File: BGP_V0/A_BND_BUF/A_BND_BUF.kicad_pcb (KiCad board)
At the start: 2 copper layers, 30 x 30 mm, 27 parts, among them J1 Conn_01x05, P1 CONN_01X02, P2 CONN_01X02, Q1 2SK208, Q2 2SK208, U1 OPA180

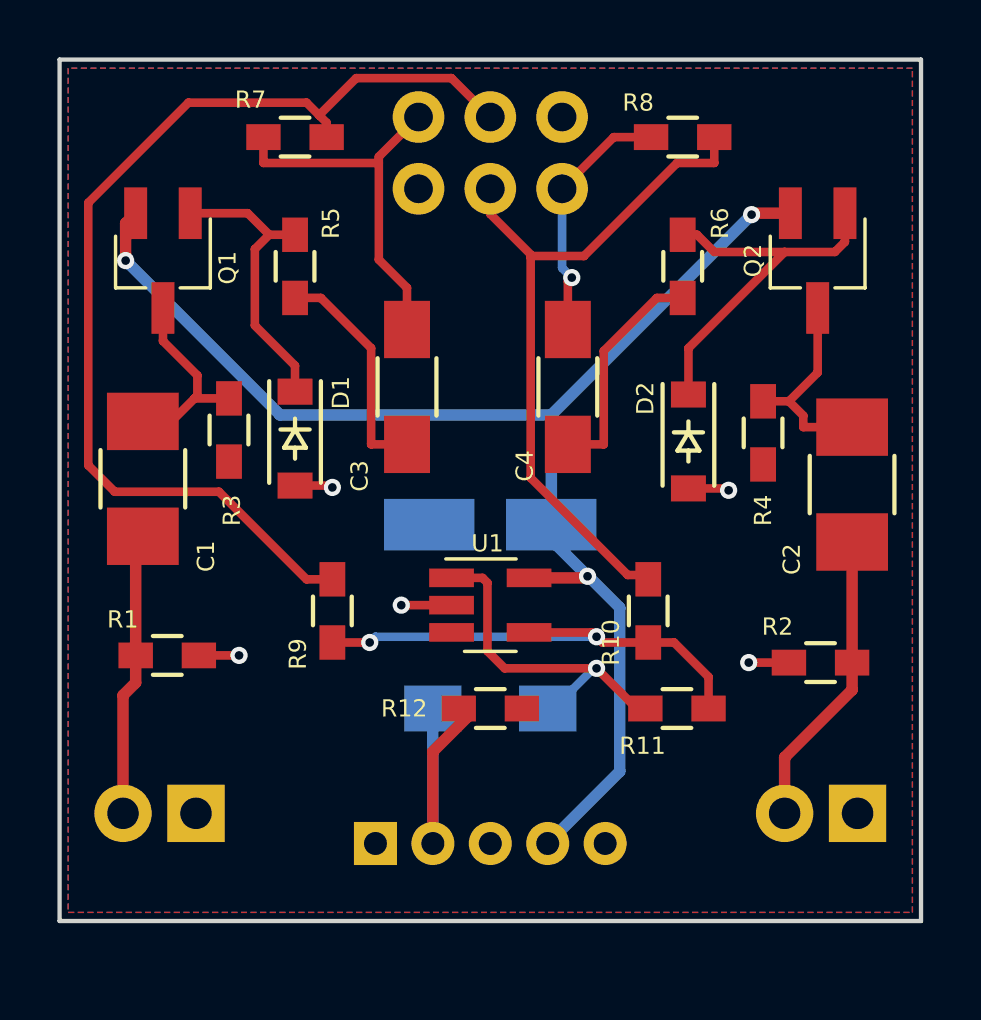
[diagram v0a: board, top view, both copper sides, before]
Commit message: Gerbers
Mainly getting gerbers ready.  Issue with pots overlapping other boards in silk screens - top and bottom.
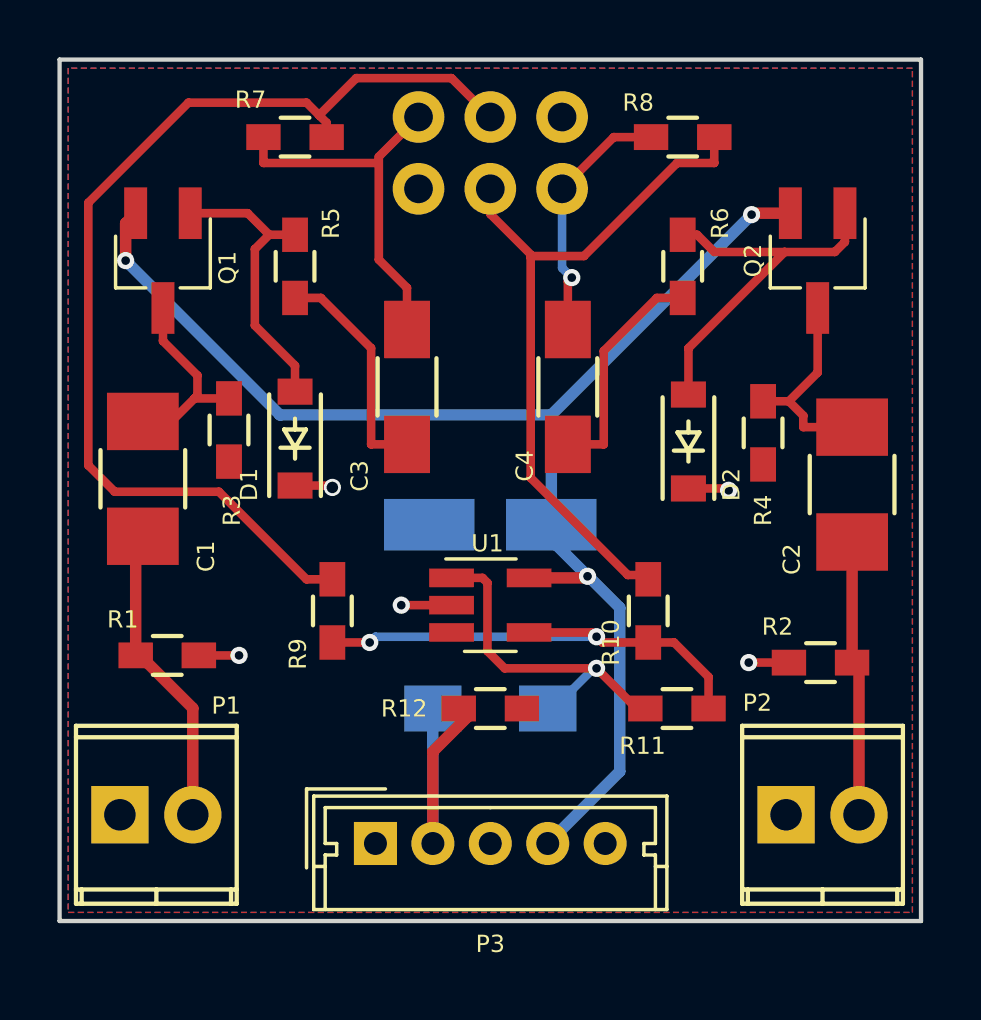
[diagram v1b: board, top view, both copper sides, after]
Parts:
- removed J1: Conn_01x05, Connectors_Molex:Molex_MicroLatch-53253-0570_05x2.00mm_Straight
- added P3: Conn_01x05, Connectors_Molex:Molex_MicroLatch-53253-0570_05x2.00mm_Straight, F.Cu at (147.0, 95.3)
- P1, P2: moved to F.Cu
- moved P1 2.65 mm to (138.1, 94.3), turned to 0 degrees
- moved P2 2.49 mm to (161.3, 94.3), turned to 0 degrees
- turned D1 to 90 degrees
- turned D2 to 90 degrees
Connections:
- D1 pad 1: Net-(D1-Pad1) -> Earth
- D1 pad 2: Earth -> Net-(D1-Pad2)
- D2 pad 1: Net-(D2-Pad1) -> Earth
- D2 pad 2: Earth -> Net-(D2-Pad2)
- Q1 pad 1: Net-(D1-Pad1) -> Net-(D1-Pad2)
- Q2 pad 1: Net-(D2-Pad1) -> Net-(D2-Pad2)
- R5 pad 2: Net-(D1-Pad1) -> Net-(D1-Pad2)
- R6 pad 2: Net-(D2-Pad1) -> Net-(D2-Pad2)
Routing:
- net Net-(D2-Pad2): track 0.00 -> 13.4 mm
- net Net-(D2-Pad1): track 13.4 -> 0.00 mm
- net Net-(D1-Pad2): track 0.00 -> 10.2 mm
- net Net-(D1-Pad1): track 10.2 -> 0.00 mm
- net Net-(C2-Pad2): track 10.4 -> 9.60 mm
- net Net-(C1-Pad2): track 9.94 -> 10.7 mm

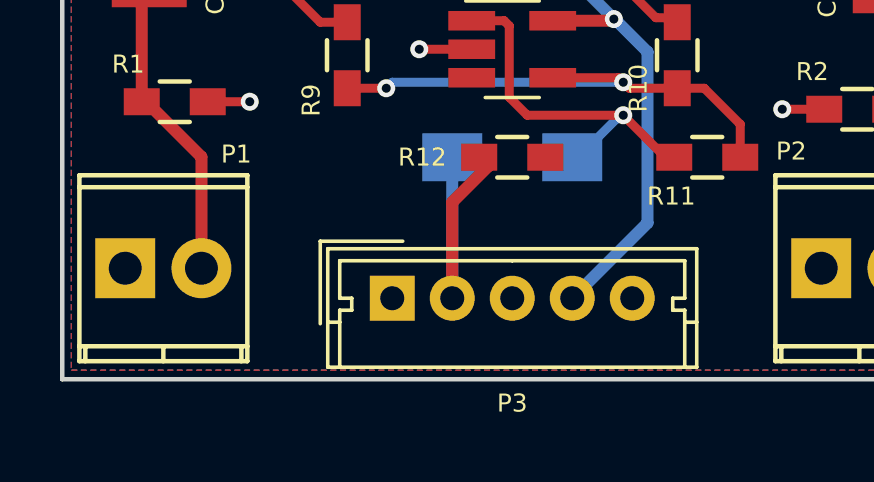
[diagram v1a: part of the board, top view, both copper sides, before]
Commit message: Pot fixups for silkscreen overlap
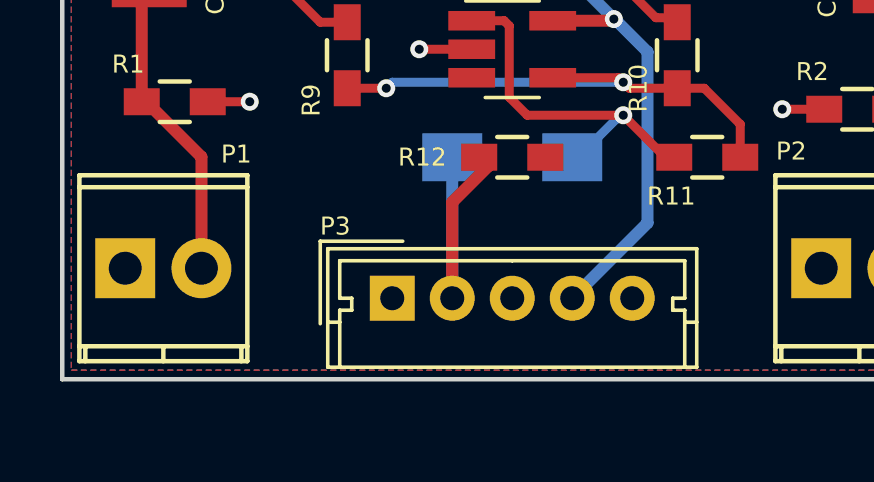
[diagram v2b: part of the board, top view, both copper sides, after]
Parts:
- RV1: footprint Potentiometers:Potentiometer_Alps_RK097_Double_Vertical -> LIBS:Potentiometer_Alps_RK097_Double_Vertical

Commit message: Concentric pot fixups for 0_BT Stack and 1_HPF
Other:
- board text added: "BGP V0.0 Buffer/Blend"
- board text removed: "BGP V1.0 BUF"
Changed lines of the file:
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@@
     (links 47)
     (no_connects 0)
-    (area 135.405 63.842857 166.075001 99.65588)
+    (area 135.405 66.185712 166.075001 99.65588)
     (thickness 1.6)
     (drawings 9)
@@
     )
   )
-  (gr_text "BGP V1.0\nBUF" (at 163 69.6) (layer B.SilkS)
+  (gr_text "BGP V0.0\nBuffer/Blend" (at 162 70) (layer B.SilkS)
     (effects (font (size 0.6 0.6) (thickness 0.15)) (justify mirror))
   )

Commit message: V_0 Updates for caps, gerbers updated
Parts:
- C1, C2: footprint Capacitors_SMD:C_1210_HandSoldering -> Capacitors_Tantalum_SMD:TantalC_SizeR_EIA-2012
- C3, C4, C5: footprint Capacitors_SMD:C_1206_HandSoldering -> Capacitors_Tantalum_SMD:TantalC_SizeS_EIA-3216
- C6: footprint Capacitors_Tantalum_SMD:TantalC_SizeB_EIA-3528_HandSoldering -> Capacitors_SMD:C_0805_HandSoldering
- moved C6 1.13 mm to (151.8, 83.3)
- moved C2 0.88 mm to (163.6, 81.9), turned to 90 degrees
- moved C1 0.78 mm to (138.8, 81.8), turned to 90 degrees
- moved C5 0.25 mm to (150.8, 90.7), turned to 0 degrees
- moved C4 0.15 mm to (153.7, 79.5), turned to 270 degrees
- moved C3 0.10 mm to (148.1, 79.5), turned to 270 degrees
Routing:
- net Net-(R7-Pad1): track 36.9 -> 31.5 mm
- net Net-(C3-Pad1): track 7.98 -> 6.19 mm
- net Net-(C2-Pad2): track 9.60 -> 11.3 mm
- net Net-(C1-Pad2): track 10.7 -> 12.3 mm
- net Net-(C3-Pad2): track 13.3 -> 14.0 mm

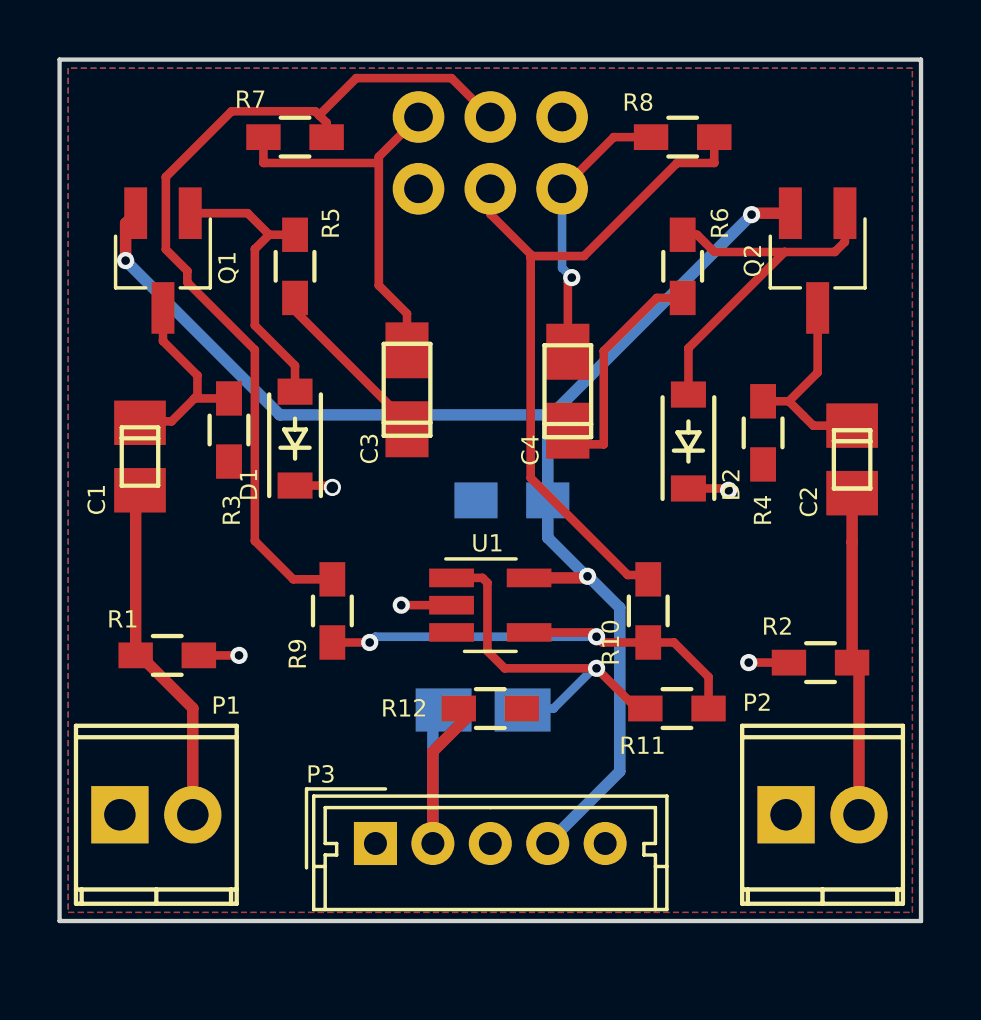
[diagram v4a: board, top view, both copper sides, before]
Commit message: V0 BUF and BT Edits
V0 Buffer change from CRD to JFET CCS. BT stack changed to reflect +/- 9V changes.
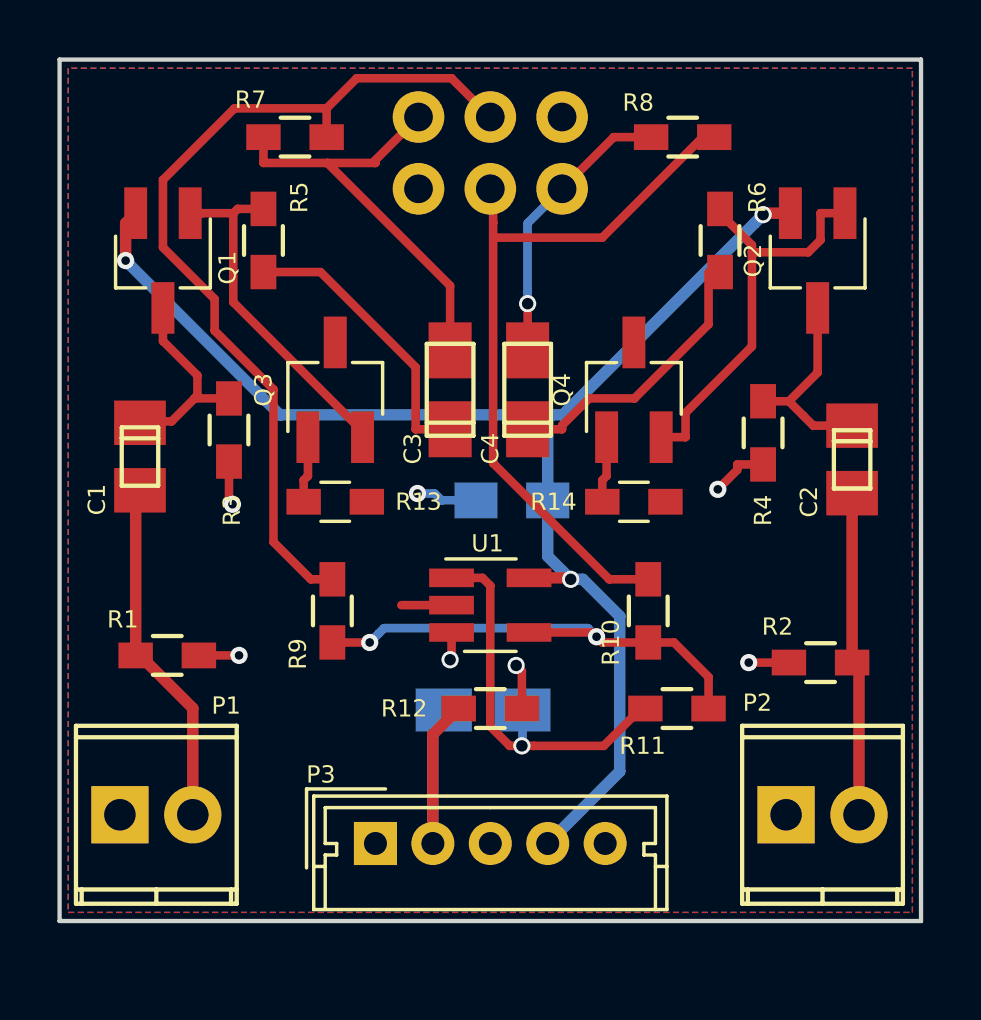
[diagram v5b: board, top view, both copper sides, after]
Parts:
- removed D1, D2: S-101, Diodes_SMD:SOD-123
- added Q3: 2SK208, TO_SOT_Packages_SMD:SC-59_Handsoldering, F.Cu at (145.6, 79.5)
- added Q4: 2SK208, TO_SOT_Packages_SMD:SC-59_Handsoldering, F.Cu at (156.0, 79.5)
- added R13: 20k, Resistors_SMD:R_0603_HandSoldering, F.Cu at (145.6, 83.4)
- added R14: 20k, Resistors_SMD:R_0603_HandSoldering, F.Cu at (156.0, 83.4)
- moved R6 1.58 mm to (159.0, 74.3)
- moved C3 1.50 mm to (149.6, 79.5)
- moved R5 1.42 mm to (143.1, 74.3)
- moved C4 1.40 mm to (152.3, 79.5)
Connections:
- C6 pad 2: Earth -> /V-
- P3 pad 1: /REF -> Earth
- P3 pad 3: Earth -> /V-
- R12 pad 2: /REF -> Earth
- R3 pad 2: /REF -> Earth
- R4 pad 2: /REF -> Earth
- RV1 pad 3: /REF -> Earth
- RV1 pad 4: /REF -> Earth
- U1 pad 2: Earth -> /V-
- U1 pad 3: /REF -> Earth
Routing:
- net /V-: track 0.00 -> 3.89 mm, vias 0 -> 1
- net Net-(C3-Pad1): track 6.19 -> 10.0 mm
- net Net-(Q4-Pad1): track 0.00 -> 2.31 mm
- net Net-(Q3-Pad1): track 0.00 -> 2.31 mm
- net Net-(Q1-Pad1): track 10.2 -> 12.3 mm
- net Net-(C4-Pad1): track 8.02 -> 9.71 mm
- net Earth: track 7.30 -> 8.94 mm, vias 5 -> 6
- net Net-(C5-Pad1): track 12.3 -> 13.9 mm
- net Net-(C3-Pad2): track 14.0 -> 15.3 mm
- net Net-(Q2-Pad1): track 13.4 -> 14.6 mm
- net Net-(C4-Pad2): track 8.94 -> 9.97 mm
- net Net-(R10-Pad2): track 24.9 -> 25.8 mm
- added copper zone on F.Cu, net /V-
- removed copper zone on F.Cu, net /REF

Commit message: Slight changes to Port layer placement - gerbers done
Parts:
- P1, P2, P3: moved to B.Cu
- moved P1 2.50 mm to (140.6, 94.3), turned to 180 degrees
- moved P2 2.50 mm to (163.8, 94.3), turned to 180 degrees
- moved P3 0.10 mm to (147.0, 95.2)
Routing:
- net Net-(C2-Pad2): track 11.3 -> 12.6 mm
- net Net-(C1-Pad2): track 12.3 -> 11.8 mm
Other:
- board text added: "+"
- board text added: "-"
- board text added: "G"
- board text added: "I"
- board text added: "O"

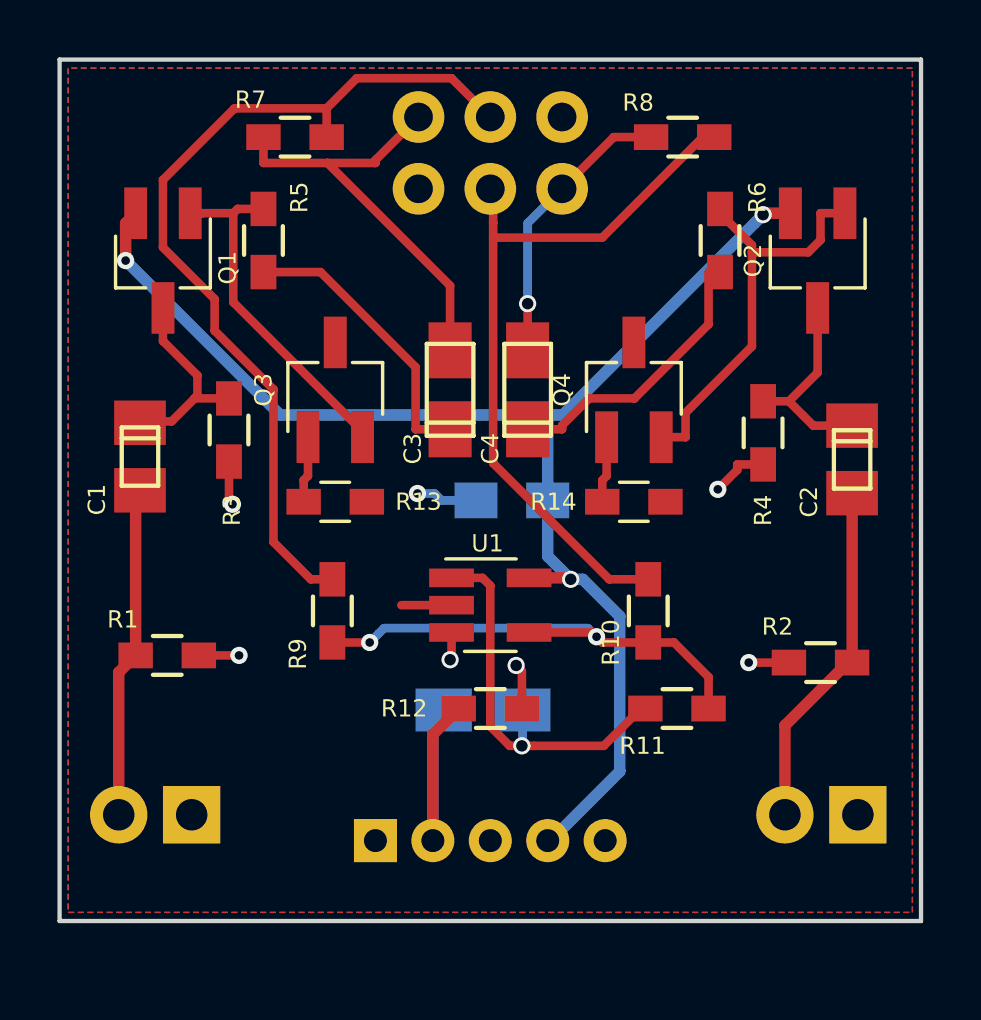
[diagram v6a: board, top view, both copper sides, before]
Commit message: Slight changes to Port layer placement - gerbers done
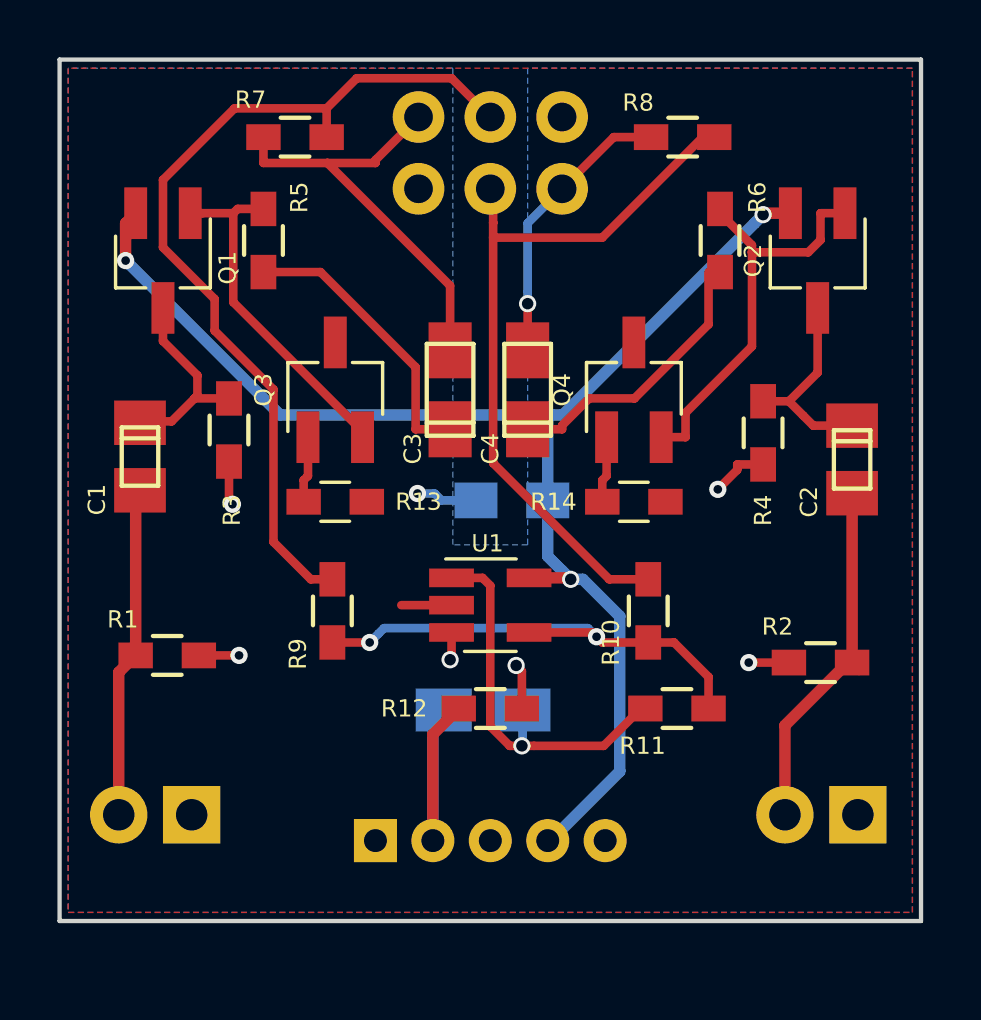
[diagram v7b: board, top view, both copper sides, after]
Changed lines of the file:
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@@
   (zone (net 10) (net_name Earth) (layer B.Cu) (hatch edge 0.508)
     (connect_pads (clearance 0.3))
-    (min_thickness 0.3)
-    (fill yes (arc_segments 16) (thermal_gap 0.3) (thermal_bridge_width 0.6))
+    (min_thickness 0.254)
+    (fill yes (arc_segments 16) (thermal_gap 0.508) (thermal_bridge_width 0.508))
     (polygon
       (pts
-        (xy 165.7 68.3) (xy 136.3 68.3) (xy 136.3 97.7) (xy 165.7 97.7)
+        (xy 165.7 68.3) (xy 152.3 68.3) (xy 152.3 84.9) (xy 149.7 84.9) (xy 149.7 68.3)
+        (xy 136.3 68.3) (xy 136.3 97.7) (xy 165.7 97.7)
       )
     )
